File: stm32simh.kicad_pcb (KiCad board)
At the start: 4 copper layers, 78.8 x 75.6 mm, 89 parts, among them J1 Micro_SD_Card_Det_Hirose_DM3AT, J2 ARM JTAG, J3 USB_C_USB2.0_16P, J4 SERIAL1, J5 RJ45, U1 STM32H753ZIT6, U2 IS61WV204816BLL-10TLI, U3 LAN8720A, U4 CP2102N, U5 LM3671 3.3V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

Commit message: cleanups
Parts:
- moved C23 4.10 mm to (136.4, 80.2)
- moved C29 3.62 mm to (126.9, 50.6), turned to -90 degrees
- moved C33 2.65 mm to (155.0, 44.2), turned to -90 degrees
- moved C17 1.00 mm to (146.2, 81.9), turned to 180 degrees
- moved C18 0.91 mm to (150.8, 81.9), turned to 180 degrees
- moved C13 0.86 mm to (150.4, 57.5), turned to 0 degrees
- moved C1 0.86 mm to (118.5, 57.7), turned to 0 degrees
- moved C11 0.82 mm to (156.9, 57.5), turned to 0 degrees
- moved C21 0.79 mm to (161.5, 62.5)
- moved C22 0.79 mm to (161.5, 61.5)
- moved C15 0.70 mm to (136.7, 66.2), turned to 90 degrees
- moved D7 0.61 mm to (182.7, 36.5)
- moved R23 0.61 mm to (182.2, 38.2)
- moved R14 0.60 mm to (144.9, 44.1)
- moved C16 0.57 mm to (136.6, 78.3), turned to 90 degrees
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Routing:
- net GND: track 91.7 -> 81.2 mm
- net +3.3V: track 81.2 -> 72.6 mm, vias 34 -> 33
- net /SRAM/D9: track 34.1 -> 30.0 mm
- net /SRAM/D10: track 35.0 -> 30.9 mm
- net Net-(U1C-ETH_TX_EN): track 48.6 -> 44.5 mm
- net /SRAM/D8: track 33.3 -> 29.3 mm
- net /SRAM/A9: track 35.3 -> 31.5 mm
- net /SRAM/D11: track 36.3 -> 32.9 mm
- net Net-(C23-Pad1): track 7.32 -> 4.67 mm, vias 2 -> 0
- net /SRAM/D0: track 37.2 -> 39.1 mm
- net /SRAM/A10: track 31.2 -> 29.6 mm
- net /SRAM/A11: track 29.3 -> 27.8 mm
- net /SDIO, Debug/SWDIO: track 28.3 -> 29.5 mm
- net Net-(U1C-ETH_REF_CLK): track 26.5 -> 27.7 mm
- net Net-(U1C-ETH_MDC): track 28.9 -> 29.7 mm
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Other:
- board text added: "+3.3V"
- board text added: "100M"
- board text added: "ACT"
- board text added: "GND"
- board text added: "JLCJLCJLCJLC"
- board text added: "RX"
- board text added: "SD"
- board text added: "SWD"
- board text added: "TX"
- board text added: "VUSB"

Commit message: VDD zone
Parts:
- added NT1: NetTie_2, NetTie:NetTie-2_SMD_Pad0.5mm, F.Cu at (161.3, 56.0)
- moved C20 25.8 mm to (162.4, 58.0)
- moved C6 10.6 mm to (143.8, 84.6), turned to 0 degrees
- moved C5 9.57 mm to (140.9, 86.1), turned to 0 degrees
- moved R1 4.70 mm to (161.3, 80.8)
- moved C4 4.70 mm to (161.3, 81.9)
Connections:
- C10 pad 1: +3.3V -> /STM32 Supplies, Reset, Config, OSC, VREF/VDD
- C11 pad 1: +3.3V -> /STM32 Supplies, Reset, Config, OSC, VREF/VDD
- C12 pad 1: +3.3V -> /STM32 Supplies, Reset, Config, OSC, VREF/VDD
- C13 pad 1: +3.3V -> /STM32 Supplies, Reset, Config, OSC, VREF/VDD
- C14 pad 1: +3.3V -> /STM32 Supplies, Reset, Config, OSC, VREF/VDD
- C15 pad 1: +3.3V -> /STM32 Supplies, Reset, Config, OSC, VREF/VDD
- C16 pad 1: +3.3V -> /STM32 Supplies, Reset, Config, OSC, VREF/VDD
- C17 pad 1: +3.3V -> /STM32 Supplies, Reset, Config, OSC, VREF/VDD
- C18 pad 1: +3.3V -> /STM32 Supplies, Reset, Config, OSC, VREF/VDD
- C19 pad 1: +3.3V -> /STM32 Supplies, Reset, Config, OSC, VREF/VDD
- C20 pad 1: +3.3V -> /STM32 Supplies, Reset, Config, OSC, VREF/VDD
- C9 pad 1: +3.3V -> /STM32 Supplies, Reset, Config, OSC, VREF/VDD
- U1 pad 108: +3.3V -> /STM32 Supplies, Reset, Config, OSC, VREF/VDD
- U1 pad 121: +3.3V -> /STM32 Supplies, Reset, Config, OSC, VREF/VDD
- U1 pad 131: +3.3V -> /STM32 Supplies, Reset, Config, OSC, VREF/VDD
- U1 pad 144: +3.3V -> /STM32 Supplies, Reset, Config, OSC, VREF/VDD
- U1 pad 17: +3.3V -> /STM32 Supplies, Reset, Config, OSC, VREF/VDD
- U1 pad 30: +3.3V -> /STM32 Supplies, Reset, Config, OSC, VREF/VDD
- U1 pad 39: +3.3V -> /STM32 Supplies, Reset, Config, OSC, VREF/VDD
- U1 pad 52: +3.3V -> /STM32 Supplies, Reset, Config, OSC, VREF/VDD
- U1 pad 62: +3.3V -> /STM32 Supplies, Reset, Config, OSC, VREF/VDD
- U1 pad 72: +3.3V -> /STM32 Supplies, Reset, Config, OSC, VREF/VDD
- U1 pad 84: +3.3V -> /STM32 Supplies, Reset, Config, OSC, VREF/VDD
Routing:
- net +3.3V: track 72.6 -> 41.6 mm, vias 33 -> 22
- net /STM32 Supplies, Reset, Config, OSC, VREF/VDD: track 0.00 -> 28.8 mm, vias 0 -> 12
- net /Ethernet/~{RESET}: track 118.3 -> 110.8 mm
- net Net-(J5-RCT): track 62.9 -> 61.0 mm
- net /SDIO, Debug/SWDIO: track 29.5 -> 28.3 mm
- net Net-(J1-DAT3/CD): track 22.4 -> 23.1 mm
- net GND: track 81.2 -> 80.4 mm
- net Net-(D1-K): track 14.3 -> 15.0 mm
- net /SRAM/D0: track 39.1 -> 38.5 mm
- net Net-(J5-RD-): track 29.9 -> 29.3 mm
- net Net-(J3-CC1): track 7.00 -> 6.47 mm
- net /SRAM/A17: track 33.1 -> 32.6 mm
- added copper zone on In2.Cu, net /STM32 Supplies, Reset, Config, OSC, VREF/VDD

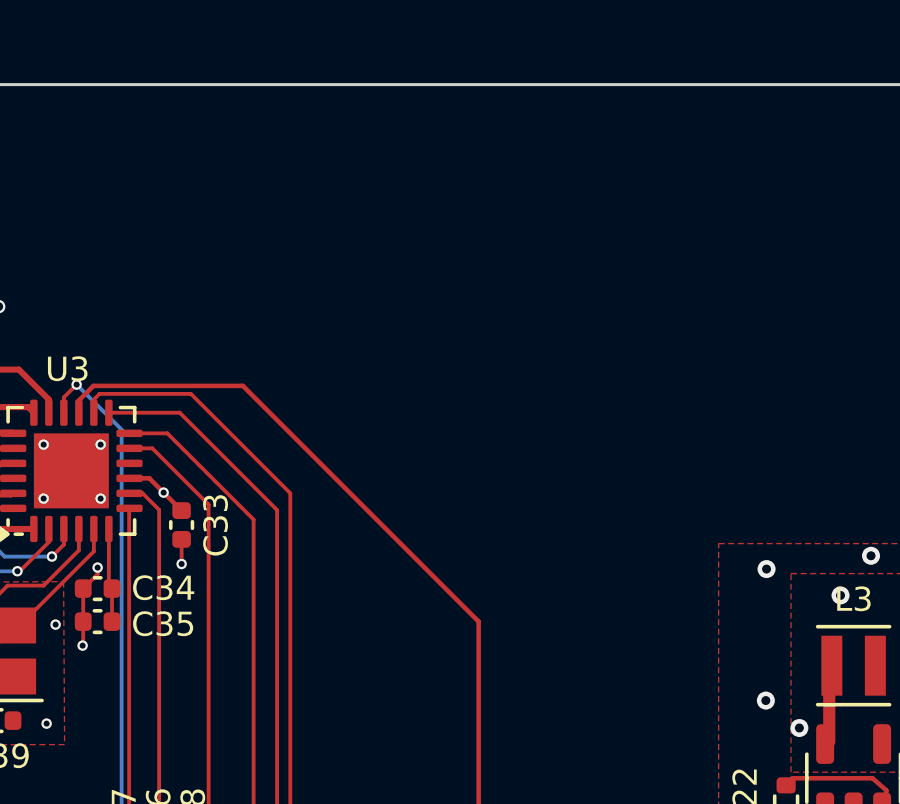
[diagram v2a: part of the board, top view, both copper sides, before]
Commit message: add reset button
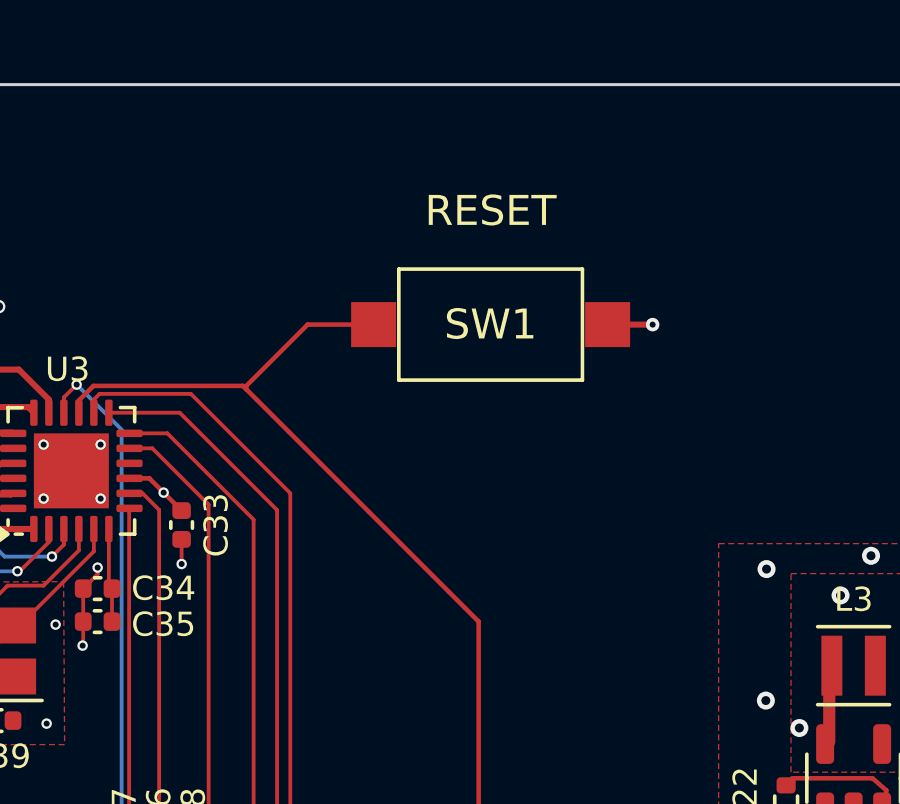
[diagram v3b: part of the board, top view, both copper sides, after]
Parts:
- added SW1: RESET, Button_Switch_SMD:SW_SPST_CK_RS282G05A3, F.Cu at (165.3, 37.5)
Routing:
- net /Ethernet/~{RESET}: track 110.8 -> 116.0 mm
- net GND: track 80.4 -> 81.9 mm, vias 77 -> 78
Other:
- board text added: "RESET"

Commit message: cleanups
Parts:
- added H1: MountingHole, MountingHole:MountingHole_2.2mm_M2_ISO14580_Pad, F.Cu at (186.2, 104.5)
- added H2: MountingHole, MountingHole:MountingHole_2.2mm_M2_ISO14580_Pad, F.Cu at (112.1, 30.9)
- added H3: MountingHole, MountingHole:MountingHole_2.2mm_M2_ISO14580_Pad, F.Cu at (186.2, 30.6)
- added H4: MountingHole, MountingHole:MountingHole_2.2mm_M2_ISO14580_Pad, F.Cu at (112.1, 104.9)
- added H6: OSHW, Symbol:OSHW-Logo_7.5x8mm_SilkScreen, F.Cu at (166.4, 41.9)
- moved SW1 10.7 mm to (174.1, 31.5)
- moved D7 3.24 mm to (179.7, 37.7)
- moved R23 3.24 mm to (179.2, 39.5)
- moved R19 0.95 mm to (135.0, 33.8)
- moved R20 0.40 mm to (135.0, 35.6)
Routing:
- net /Ethernet/~{RESET}: track 116.0 -> 127.3 mm
- net Net-(J5-TD-): track 28.1 -> 27.5 mm
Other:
- board size 78.8 x 75.6 mm -> 80 x 80 mm

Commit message: align holes
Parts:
- moved H1 0.40 mm to (186.2, 104.9)
- moved H3 0.30 mm to (186.2, 30.9)
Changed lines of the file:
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@@
 	(footprint "MountingHole:MountingHole_2.2mm_M2_ISO14580_Pad"
 		(layer "F.Cu")
-		(at 186.2 30.6)
+		(at 186.2 30.9)
 		(descr "Mounting Hole 2.2mm, M2, ISO14580")
 		(tags "mounting hole 2.2mm m2 iso14580")
@@
 	(footprint "MountingHole:MountingHole_2.2mm_M2_ISO14580_Pad"
 		(layer "F.Cu")
-		(at 186.2 104.5)
+		(at 186.2 104.9)
 		(descr "Mounting Hole 2.2mm, M2, ISO14580")
 		(tags "mounting hole 2.2mm m2 iso14580")
@@
 		(polygon
 			(pts
-				(xy 109.5 28.3) (xy 188.9 28.1) (xy 189.4 107.55) (xy 110 107.5)
+				(xy 109.5 28.3) (xy 188.9 28.1) (xy 188.9 107.6) (xy 109.5 107.3)
 			)
 		)
